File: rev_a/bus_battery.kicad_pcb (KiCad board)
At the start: 2 copper layers, 50 x 50 mm, 4 parts

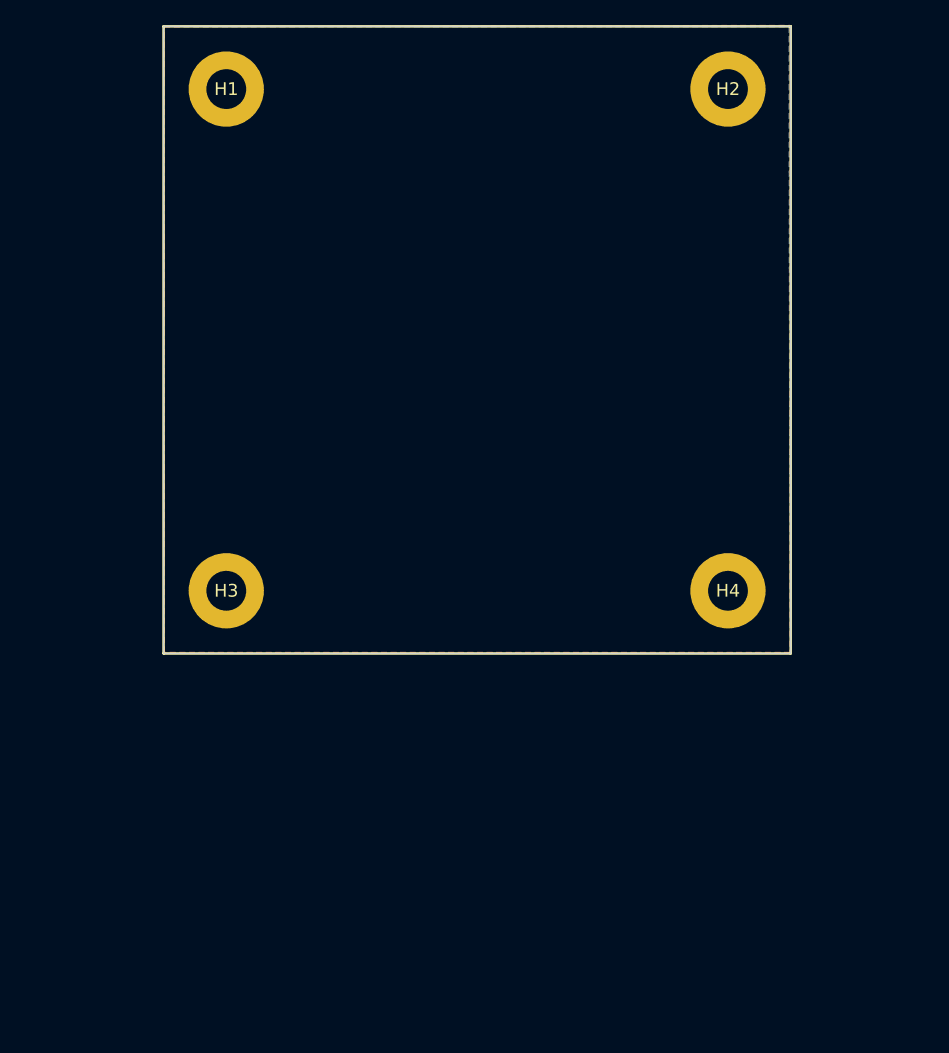
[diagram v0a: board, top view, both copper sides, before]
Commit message: Concluded that this will have to be a 5cm x 10cm board.
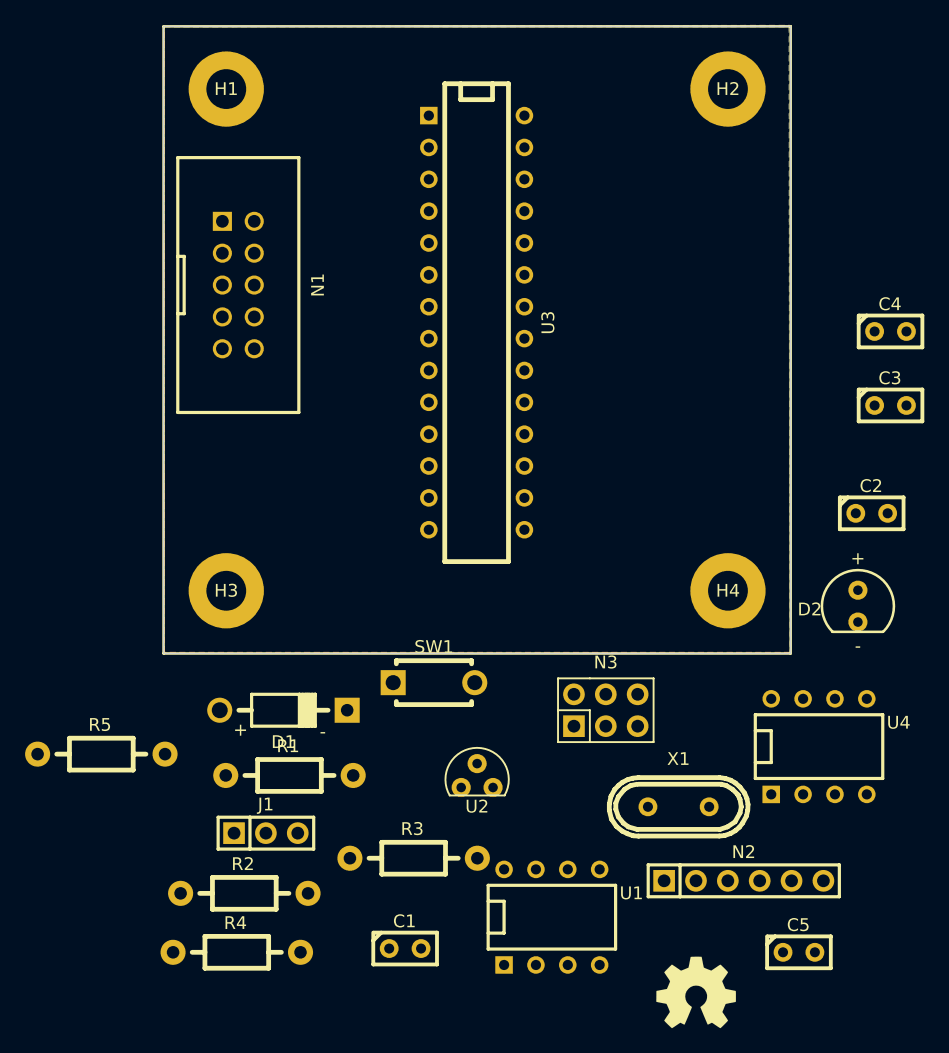
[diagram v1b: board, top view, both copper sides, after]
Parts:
- added C1: 18pF, Bus_Battery:Capacitor3MMDiscRM2.5, F.Cu at (119.3, 173.5)
- added C2: .1uF, Bus_Battery:Capacitor3MMDiscRM2.5, F.Cu at (156.5, 138.8)
- added C3: 1uF, Bus_Battery:Capacitor3MMDiscRM2.5, F.Cu at (158.0, 130.2)
- added C4: 18pF, Bus_Battery:Capacitor3MMDiscRM2.5, F.Cu at (158.0, 124.3)
- added C5: 1uF, Bus_Battery:Capacitor3MMDiscRM2.5, F.Cu at (150.7, 173.8)
- added D1: SD101C-TR, Bus_Battery:Diode_DO-41_SOD81_Horizontal_RM10, F.Cu at (109.6, 154.5)
- added D2: LED, Bus_Battery:T1_LED, F.Cu at (155.4, 146.2)
- added G1: OSHW_LOGO, Bus_Battery:OSHW_LOGO_250mil, F.Cu at (142.5, 177.0)
- added J1: TERMINATE_JUMPER, Bus_Battery:Pin_Header_Straight_1x03, F.Cu at (108.2, 164.3)
- added N1: BUS_SLAVE_HEADER, Bus_Battery:Pin_Header_Straight_2x05_Shrouded, F.Cu at (106.0, 120.6)
- added N2: FTDI_HEADER, Bus_Battery:Pin_Header_Straight_1x06, F.Cu at (146.3, 168.1)
- added N3: AVR_ISP_HEADER, Bus_Battery:Pin_Header_Straight_2x03, F.Cu at (135.3, 154.5)
- added R1: 120, Bus_Battery:Resistor_Horizontal_RM10mm, F.Cu at (110.0, 159.7)
- added R2: 10K, Bus_Battery:Resistor_Horizontal_RM10mm, F.Cu at (106.4, 169.1)
- added R3: 1K, Bus_Battery:Resistor_Horizontal_RM10mm, F.Cu at (119.9, 166.3)
- added R4: 1K, Bus_Battery:Resistor_Horizontal_RM10mm, F.Cu at (105.8, 173.8)
- added R5: 470, Bus_Battery:Resistor_Horizontal_RM10mm, F.Cu at (95.0, 158.0)
- added SW1: 2_LEAD_PUSH_BUTTON, Bus_Battery:Button_6.5MM, F.Cu at (121.6, 152.3)
- added U1: MCP2562, Bus_Battery:DIP-8__300, F.Cu at (131.0, 171.0)
- added U2: L78L05AC, Bus_Battery:TO92_123, F.Cu at (125.0, 160.1)
- added U3: ATMEGA328_DIP28, Bus_Battery:DIP-28__300, F.Cu at (125.0, 123.6)
- added U4: OPTO_ISOLATOR, Bus_Battery:DIP-8__300, F.Cu at (152.3, 157.4)
- added X1: CRYSTAL, Bus_Battery:Crystal_HC49-U_Vertical, F.Cu at (141.1, 162.2)

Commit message: Finished off Rev. A.
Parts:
- added C10: .1uF, Bus_Battery:Capacitor3MMDiscRM2.5, F.Cu at (118.1, 139.7)
- added C6: .1uF, Bus_Battery:Capacitor3MMDiscRM2.5, F.Cu at (113.0, 121.9)
- added C7: .1uF, Bus_Battery:Capacitor3MMDiscRM2.5, F.Cu at (119.4, 107.3)
- added C8: .1uF, Bus_Battery:Capacitor3MMDiscRM2.5, F.Cu at (137.2, 146.7)
- added C9: .1uF, Bus_Battery:Capacitor3MMDiscRM2.5, F.Cu at (137.2, 141.6)
- added R10: 82K, Bus_Battery:R_HORIZ_300, F.Cu at (134.6, 144.1)
- added R11: 10K, Bus_Battery:R_HORIZ_300, F.Cu at (134.6, 132.7)
- added R6: 10K, Bus_Battery:R_HORIZ_300, F.Cu at (118.1, 145.4)
- added R7: 220, Bus_Battery:Pin_Header_Straight_1x06, F.Cu at (137.2, 130.2)
- added R8: 470, Bus_Battery:R_HORIZ_300, F.Cu at (118.1, 142.9)
- added R9: 470, Bus_Battery:R_HORIZ_300, F.Cu at (114.3, 101.6)
- added U5: ATMEGA328_DIP28, Bus_Battery:DIP-28__300, F.Cu at (119.4, 113.7)
- added U6: LTV-816, Bus_Battery:DIP-8__300, F.Cu at (128.3, 144.1)
- added U7: MCP6321_DIP8, Bus_Battery:DIP-8__300, F.Cu at (144.1, 135.3)
- C1: value 18pF -> .1uF
- C2: value .1uF -> 18pF
- G1: footprint Bus_Battery:OSHW_LOGO_250mil -> Bus_Battery:OSHW_LOGO_150mil; moved to B.Cu
- R1: value 120 -> 10K; footprint Bus_Battery:Resistor_Horizontal_RM10mm -> Bus_Battery:R_HORIZ_300
- R2: value 10K -> 120; footprint Bus_Battery:Resistor_Horizontal_RM10mm -> Bus_Battery:R_HORIZ_300
- R3: footprint Bus_Battery:Resistor_Horizontal_RM10mm -> Bus_Battery:R_HORIZ_300
- R4: value 1K -> 470; footprint Bus_Battery:Resistor_Horizontal_RM10mm -> Bus_Battery:R_HORIZ_300
- R5: value 470 -> 82K; footprint Bus_Battery:Resistor_Horizontal_RM10mm -> Bus_Battery:R_HORIZ_300
- U1: value MCP2562 -> L78L05AC; footprint Bus_Battery:DIP-8__300 -> Bus_Battery:TO92_123
- U2: value L78L05AC -> MCP2562; footprint Bus_Battery:TO92_123 -> Bus_Battery:DIP-8__300
- U3: value ATMEGA328_DIP28 -> L78L33AC; footprint Bus_Battery:DIP-28__300 -> Bus_Battery:TO92_123
- U4: value OPTO_ISOLATOR -> LTV-816
- moved G1 69.1 mm to (139.7, 108.0), turned to 180 degrees
- moved D2 58.4 mm to (113.0, 106.0)
- moved N2 57.0 mm to (101.6, 132.7), turned to 90 degrees
- moved C1 54.5 mm to (101.6, 121.9), turned to 90 degrees
- moved C5 53.1 mm to (128.3, 125.7)
- moved N3 52.4 mm to (126.4, 102.9)
- moved SW1 52.1 mm to (135.9, 102.2), turned to 180 degrees
- moved U1 49.8 mm to (134.0, 121.3), turned to 90 degrees
- moved X1 45.9 mm to (120.8, 121.0)
- moved R3 43.7 mm to (109.9, 123.8), turned to 90 degrees
- moved C2 40.9 mm to (118.0, 125.1), turned to 180 degrees
- moved N1 38.8 mm to (144.8, 119.4)
- moved R4 38.7 mm to (109.2, 135.3), turned to 270 degrees
- moved R1 36.0 mm to (107.3, 123.8), turned to 270 degrees
- moved C4 34.8 mm to (123.2, 125.1)
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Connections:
- net Net-(N1-Pad7) renamed /BGND
- C1 pad 2: GND -> /~RESET
- C2 pad 2: Net-(C2-Pad2) -> GND
- C3 pad 1: Net-(C3-Pad1) -> /LPWR
- D1 pad +: Net-(C2-Pad2) -> /~RESET
- D1 pad -: +5V -> +3.3V
- N1 pad 1: Net-(C3-Pad1) -> /LPWR
- N1 pad 10: Net-(N1-Pad10) -> /BPWR
- N1 pad 2: Net-(C3-Pad1) -> /LPWR
- N1 pad 9: Net-(N1-Pad10) -> /BPWR
- N2 pad 6: Net-(C2-Pad1) -> Net-(C1-Pad1)
- N3 pad 2: +5V -> +3.3V
- N3 pad 5: Net-(C2-Pad2) -> /~RESET
- R1 pad 1: Net-(N1-Pad5) -> /~RESET
- R1 pad 2: Net-(J1-Pad2) -> +3.3V
- R2 pad 1: Net-(C2-Pad2) -> Net-(N1-Pad5)
- R2 pad 2: +5V -> Net-(J1-Pad2)
- R4 pad 1: Net-(R4-Pad1) -> GND
- R4 pad 2: Net-(N2-Pad5) -> Net-(R4-Pad2)
- R5 pad 1: Net-(R5-Pad1) -> /LVOLT
- R5 pad 2: Net-(D2-Pad+) -> /SW_LPWR
- SW1 pad 2: Net-(C2-Pad2) -> /~RESET
- U1 pad 1: Net-(R3-Pad1) -> +5V
- U1 pad 3: +5V -> /LPWR
- U2 pad 1: +5V -> Net-(N2-Pad5)
- U2 pad 3: Net-(C3-Pad1) -> +5V
- U3 pad 1: Net-(C2-Pad2) -> +3.3V
- U3 pad 2: Net-(N2-Pad4) -> GND
- U3 pad 3: Net-(N2-Pad5) -> +5V
- U4 pad 1: (no net) -> Net-(U4-Pad1)
- U4 pad 2: (no net) -> Net-(R4-Pad2)
- U4 pad 3: (no net) -> Net-(U4-Pad3)
- U4 pad 4: (no net) -> Net-(R8-Pad2)
- U4 pad 5: (no net) -> /SW_BPWR
- U4 pad 6: (no net) -> /BPWR
- U4 pad 7: (no net) -> /SW_LPWR
- U4 pad 8: (no net) -> /LPWR
- X1 pad 1: Net-(C1-Pad1) -> Net-(C2-Pad1)
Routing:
- net GND: track 0.00 -> 165.1 mm, vias 0 -> 28
- net +3.3V: track 0.00 -> 82.6 mm
- net /BVOLT: track 0.00 -> 67.1 mm, vias 0 -> 1
- net Net-(J1-Pad1): track 0.00 -> 49.5 mm, vias 0 -> 1
- net /~RESET: track 0.00 -> 49.0 mm, vias 0 -> 1
- net +5V: track 0.00 -> 47.6 mm
- net /BGND: track 0.00 -> 47.4 mm, vias 0 -> 5
- net /LVOLT: track 0.00 -> 44.1 mm
- net Net-(N1-Pad5): track 0.00 -> 39.3 mm, vias 0 -> 1
- net Net-(N2-Pad5): track 0.00 -> 34.3 mm
- net /SW_BPWR: track 0.00 -> 33.7 mm
- net Net-(U4-Pad3): track 0.00 -> 29.3 mm
- net /SW_LPWR: track 0.00 -> 29.2 mm, vias 0 -> 1
- net Net-(U4-Pad1): track 0.00 -> 27.4 mm
- net Net-(C9-Pad2): track 0.00 -> 27.4 mm
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- added copper zone on B.Cu, net /BGND
- added copper zone on F.Cu, net /BGND
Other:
- board text added: "+"
- board text added: "-"
- board text added: "1"
- board text added: "BUS_BATTERY REV. A (c) 2015 BY GRAMLICH"
- board text added: "BUS_BATTERY REV. A 26JAN2015 COPYRIGHT (C) 2015 BY WAYNE GRAMLICH"
- board text added: "OFF"
- board text added: "ON"
- board text added: "RESET"
- board text added: "TERM"
- board text added: "hardware"
- board text added: "open source"
